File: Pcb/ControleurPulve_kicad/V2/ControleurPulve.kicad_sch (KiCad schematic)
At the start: 89 parts, among them J1 Screw_Terminal_01x02, J10 Screw_Terminal_01x04, J11 Screw_Terminal_01x04, J12 Conn_01x03_Pin, J13 Conn_01x03_Pin, J14 Conn_01x03_Pin, J15 Conn_01x03_Pin, J16 Screw_Terminal_01x04, J17 Screw_Terminal_01x04, J18 Conn_01x03_Pin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

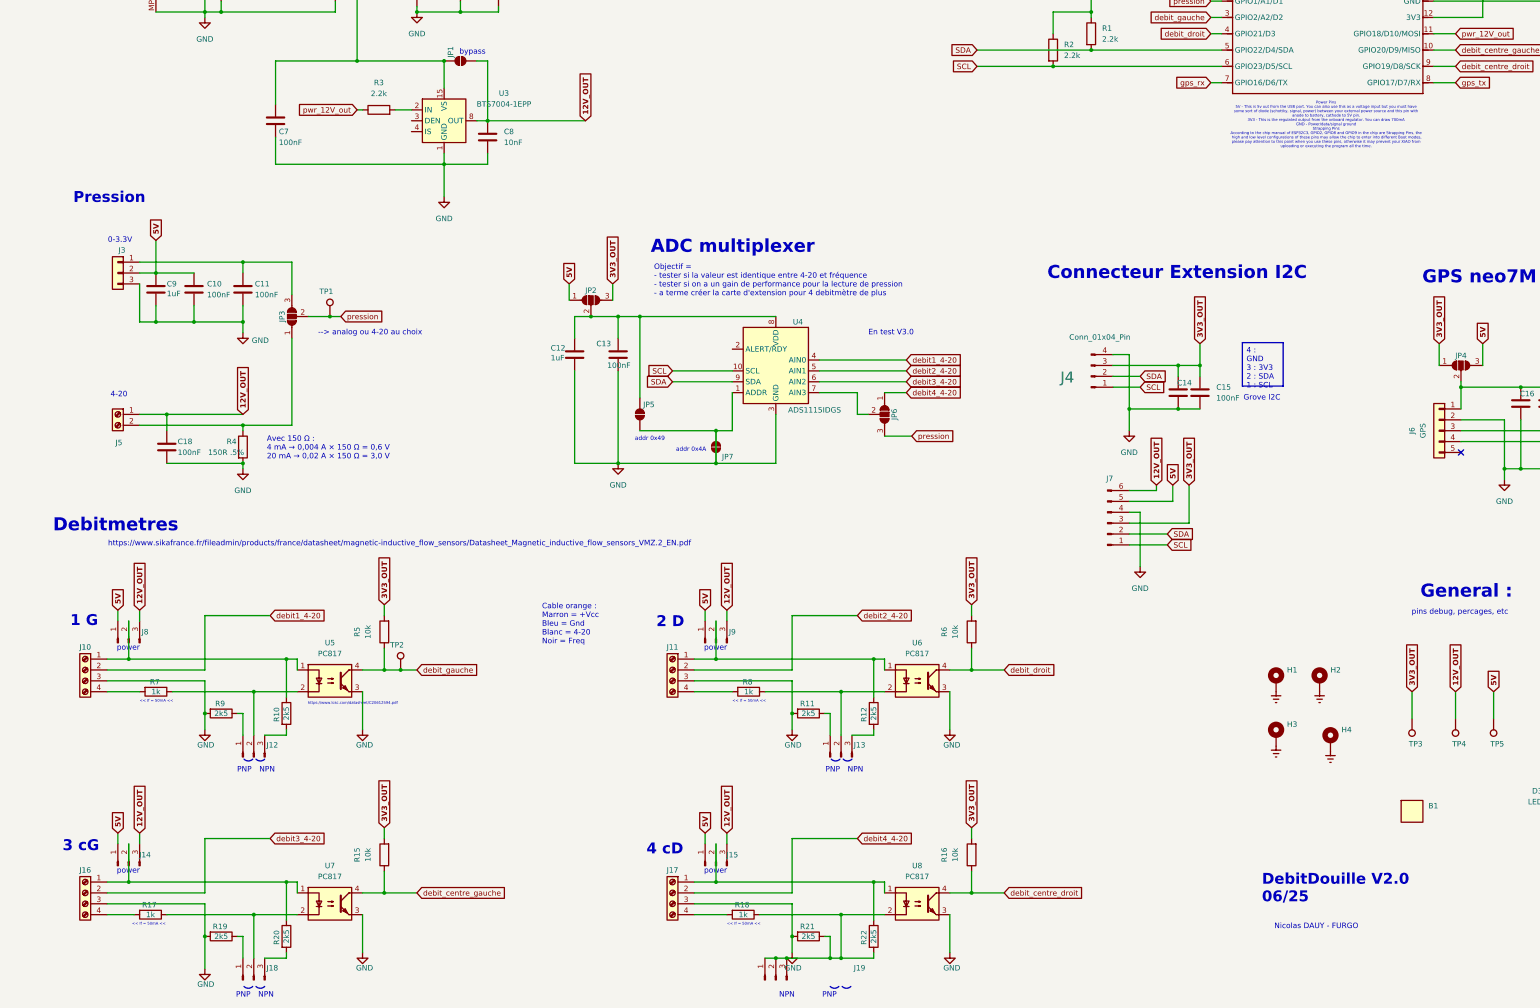
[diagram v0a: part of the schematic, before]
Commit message: PCB : silkscreen et placement (non routé)
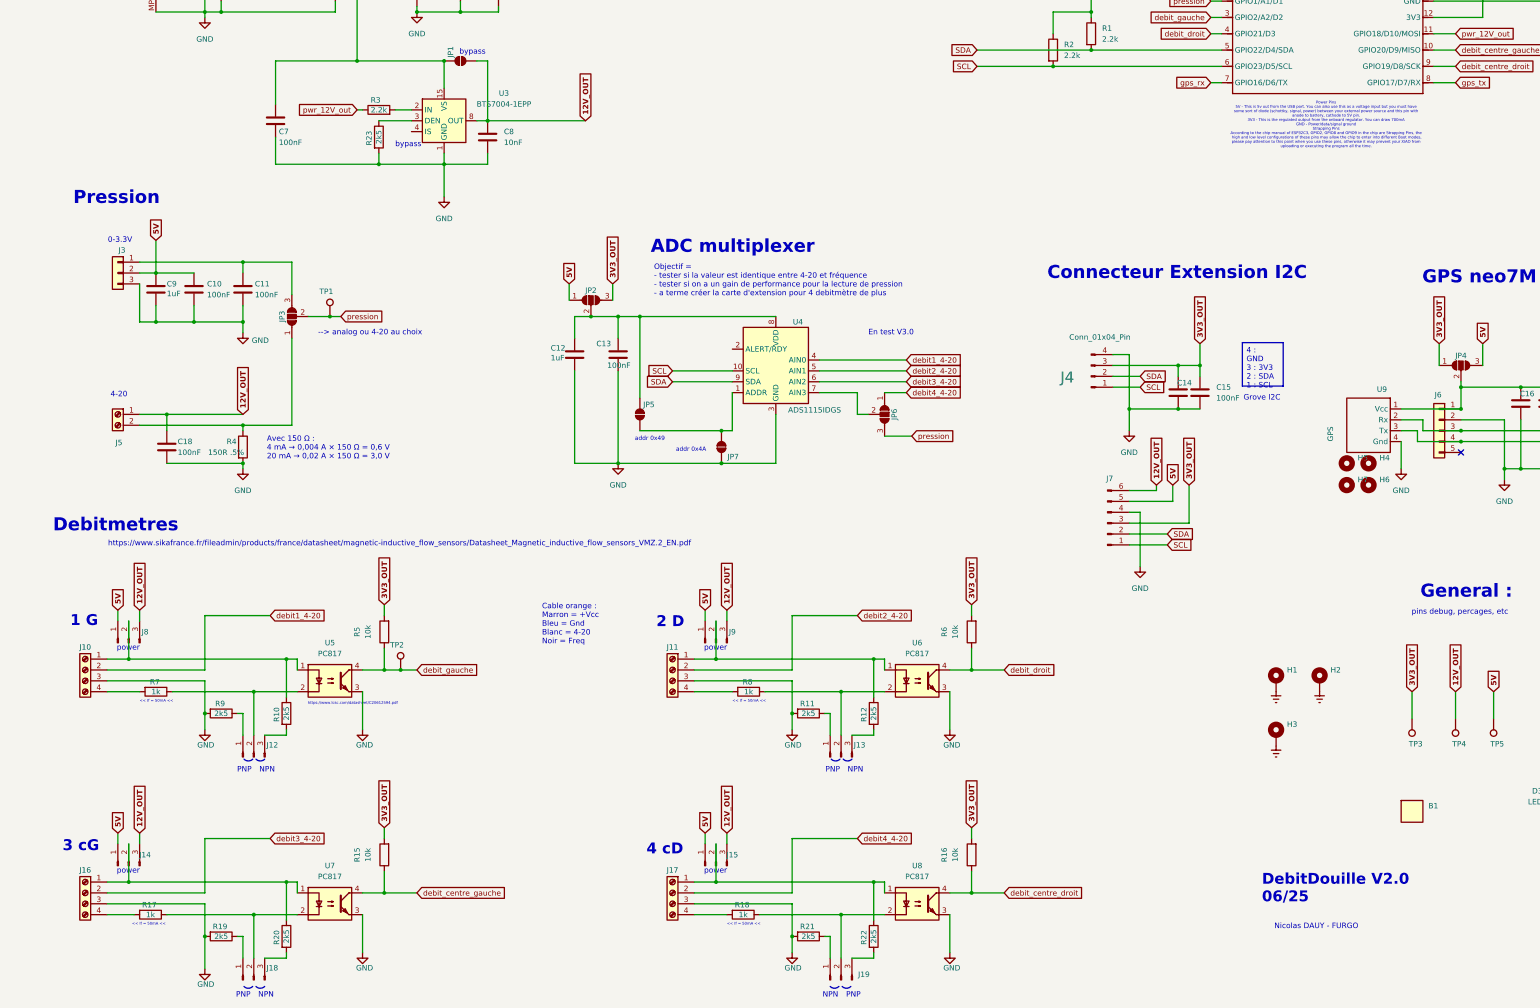
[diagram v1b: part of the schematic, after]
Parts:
- removed H4: ~, MountingHole:MountingHole_4.3mm_M4_DIN965_Pad_TopBottom, symbol Mechanical:MountingHole_Pad_MP
- added H4, H5, H6, H7: e, MountingHole:MountingHole_3.2mm_M3, symbol Mechanical:MountingHole
- added R23: 2k5, Resistor_SMD:R_0603_1608Metric, symbol Device:R
- added U9: ~, DIY_Modules:GY-NEO6MV2_25_36, symbol diy-modules1.8:GY-NEO6MV2
- J1: footprint TerminalBlock_RND:TerminalBlock_RND_205-00287_1x02_P5.08mm_Horizontal -> TerminalBlock_Phoenix:TerminalBlock_Phoenix_MKDS-1,5-2-5.08_1x02_P5.08mm_Horizontal
- J7: footprint Connector_PinSocket_2.54mm:PinSocket_1x06_P2.54mm_Vertical -> Connector_JST:JST_XH_B6B-XH-A_1x06_P2.50mm_Vertical
- R4: footprint Resistor_SMD:R_1206_3216Metric -> Resistor_SMD:R_0805_2012Metric
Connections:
- net GND: now also R23.2, U9.4 (Gnd); no longer JP5.1 (A), JP7.1 (A), U4.1 (ADDR)
- net gps_rx: now also U9.3 (Tx)
- net gps_tx: now also U9.2 (Rx)
- net at C16.1, C17.1, J6.1 (Pin_1)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: now also U9.1 (Vcc)
- net at U3.3 (DEN): now also R23.1
- new net: JP5.1 (A), JP7.1 (A), U4.1 (ADDR)
- new net: J19.2 (Pin_2), R18.1, U8.2
- new net: J19.3 (Pin_3), R22.2
- new net: J19.1 (Pin_1), R21.1
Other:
- moved on the sheet: J19, JP7

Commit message: Mise en prod
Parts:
- added D5: red, LED_SMD:LED_0603_1608Metric_Pad1.05x0.95mm_HandSolder, symbol Device:LED
- added FID1, FID2, FID3: Fiducial, Fiducial:Fiducial_0.5mm_Mask1.5mm, symbol Mechanical:Fiducial
- added R24: 2.2k, Resistor_SMD:R_0603_1608Metric_Pad0.98x0.95mm_HandSolder, symbol Device:R
- B1, J2, J3, J6, J7, TP1, TP2, TP3, TP4, TP5, U2, U9: now left out of the parts list
- C1, C13, C4, C7: LCSC (none) -> C1591; MPN (none) -> CL10B104KB8NNNC
- C10, C11, C18: LCSC C1589 -> C1591; MPN (none) -> CL10B104KB8NNNC
- C12, C9: LCSC C1589 -> C14663; MPN (none) -> CC0603KRX7R9BB104
- C14, C16: LCSC C77040 -> C2932476; MPN (none) -> CL21A106KBYQNNE
- C15, C17: LCSC C5445386 -> C1591; MPN (none) -> CL10B104KB8NNNC
- C2: LCSC (none) -> C4054388; MPN (none) -> VP1H221M0810
- C3: value 10uF -> 10uF X5R; LCSC (none) -> C2932476; MPN (none) -> CL21A106KBYQNNE
- C5: value C -> 100nF; LCSC (none) -> C1591; MPN (none) -> CL10B104KB8NNNC
- C6: value C -> 10uF X5R; LCSC (none) -> C2932476; MPN (none) -> CL21A106KBYQNNE
- C8: footprint Capacitor_SMD:C_0805_2012Metric -> Capacitor_SMD:C_0603_1608Metric; LCSC (none) -> C5137477; MPN (none) -> FCC0603B103K500CT
- D1: LCSC (none) -> C40324; MPN (none) -> MRA4004T3G
- D2: MPN (none) -> LESD5D5.0CT1G
- D3: value LED -> green; LCSC (none) -> C19273151; MPN (none) -> YLED0603G; now in the parts list
- D4: value LED -> blue; LCSC (none) -> C19171394; MPN (none) -> YLED0603B; now in the parts list
- F1: LCSC (none) -> C12559; MPN (none) -> SMD1812P050TF/30
- H1, H2, H3: footprint MountingHole:MountingHole_4.3mm_M4_DIN965_Pad_TopBottom -> MountingHole:MountingHole_3.2mm_M3_DIN965_Pad
- J1: LCSC (none) -> C8465
- J10, J11, J16, J17: LCSC (none) -> C42377749; MPN (none) -> WJ500V-5.08-4p
- J12, J13, J14, J15, J18, J19, J8, J9: LCSC (none) -> C6332196; MPN (none) -> HB-PH3-25413PB2GOP
- J5: LCSC (none) -> C784940
- JP1: footprint Jumper:SolderJumper-2_P1.3mm_Open_TrianglePad1.0x1.5mm -> Jumper:SolderJumper-2_P1.3mm_Open_RoundedPad1.0x1.5mm
- R1, R2, R3: MPN (none) -> RC0603FR-072K2L
- R10, R11, R12, R19, R20, R21, R22, R23, R9: LCSC (none) -> C304065; MPN (none) -> AR03BTC2501
- R13, R14: LCSC C107696 -> C114662; MPN (none) -> RC0603FR-072K2L
- R15, R16, R5, R6: LCSC (none) -> C98220; MPN (none) -> RC0603FR-0710kL
- R17, R18, R7, R8: LCSC (none) -> C22548; MPN (none) -> RC0603FR-071kL
- R4: value 150R .5% -> 150R .1%; LCSC (none) -> C351609; MPN (none) -> PTFR0805B150RN9
- U1: LCSC (none) -> C5198099; MPN (none) -> TSR2-2450
- U3: LCSC (none) -> C534825; MPN (none) -> BTS7004-1EPP
- U4: LCSC (none) -> C37593; MPN (none) -> ADS1115IDGSR
- U5, U6, U7, U8: footprint Package_DIP:DIP-4_W7.62mm_SMDSocket_SmallPads -> Package_DIP:DIP-4_W8.89mm_SMDSocket_LongPads; LCSC (none) -> C20612591; MPN (none) -> PC817CS
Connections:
- net GND: now also D5.1 (K)
- net ESP_LED: now reaches U2.1 (GPIO0/A0/D0)
- net ESP_LED: now also R24.1
- new net: D5.2 (A), R24.2
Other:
- note added: "General"
- note added: "unused"
- note removed: "General :"
- moved on the sheet: C14, C15, C16, C17, H4, H5, H6, H7, J4, J6, J7, JP4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

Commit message: Dév PCB : en cours de validation PCB reçus Code V2
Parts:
- removed U2: XIAO-ESP32-C6, Esp32-XIAO:XIAO-ESP32C6-DIP, symbol esp32-xiao:XIAO_ESP32-C6-DIP
- added R25, R26, R27, R28: 150R-->100R .1%, Resistor_SMD:R_0805_2012Metric, symbol Device:R
- added U10: XIAO-ESP32-S3-DIP, Esp32-XIAO:XIAO-ESP32S3-DIP, symbol esp32-xiao:XIAO-ESP32-S3-DIP
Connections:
- net 3V3_OUT: now also U10.12 (VCC_3V3)
- net 5V: now also U10.14 (VBUS)
- net ESP_LED: now also U10.1 (GPIO1/D0/A0)
- net GND: now also R25.2, R26.2, R27.2, R28.2, U10.13 (GND)
- net SCL: now also U10.6 (GPIO9/D5/I2C_SCL)
- net SDA: now also U10.5 (GPIO5/D4/I2C_SDA)
- net debit1_4-20: now also R25.1
- net debit2_4-20: now also R26.1
- net debit3_4-20: now also R28.1
- net debit4_4-20: now also R27.1
- net debit_centre_droit: now also U10.9 (GPIO7/D8/A8/SCK)
- net debit_centre_gauche: now also U10.10 (GPIO8/D9/A9/MISO)
- net debit_droit: now also U10.4 (GPIO4/D3/A3)
- net debit_gauche: now also U10.3 (GPIO3/D2/A2)
- net gps_rx: now also U10.7 (U0TXD/D6/TX)
- net gps_tx: now also U10.8 (U0RXD/D7/RX)
- net pression: now also U10.2 (GPIO2/DA/A1)
- net pwr_12V_out: now also U10.11 (GPIO9/D10/A10/MOSI)
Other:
- note added: "/!\ plusieurs modèles choisis ne pas se fier au pinout, consulter la datasheet"
- note added: "Black"
- note added: "Blue"
- note added: "Brown"
- note added: "GPIO6"
- note added: "Microcontroleur"
- note added: "White"
- note added: "i"
- note removed: "Microntonroleur"
- moved on the sheet: C1, C14, C15, C2, C3, C4, C5, C6, C7, C8, D1, D2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
